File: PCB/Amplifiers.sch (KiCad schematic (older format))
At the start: 33 parts, among them U10 TL084_v, U11 LM358, U12 TL084_v

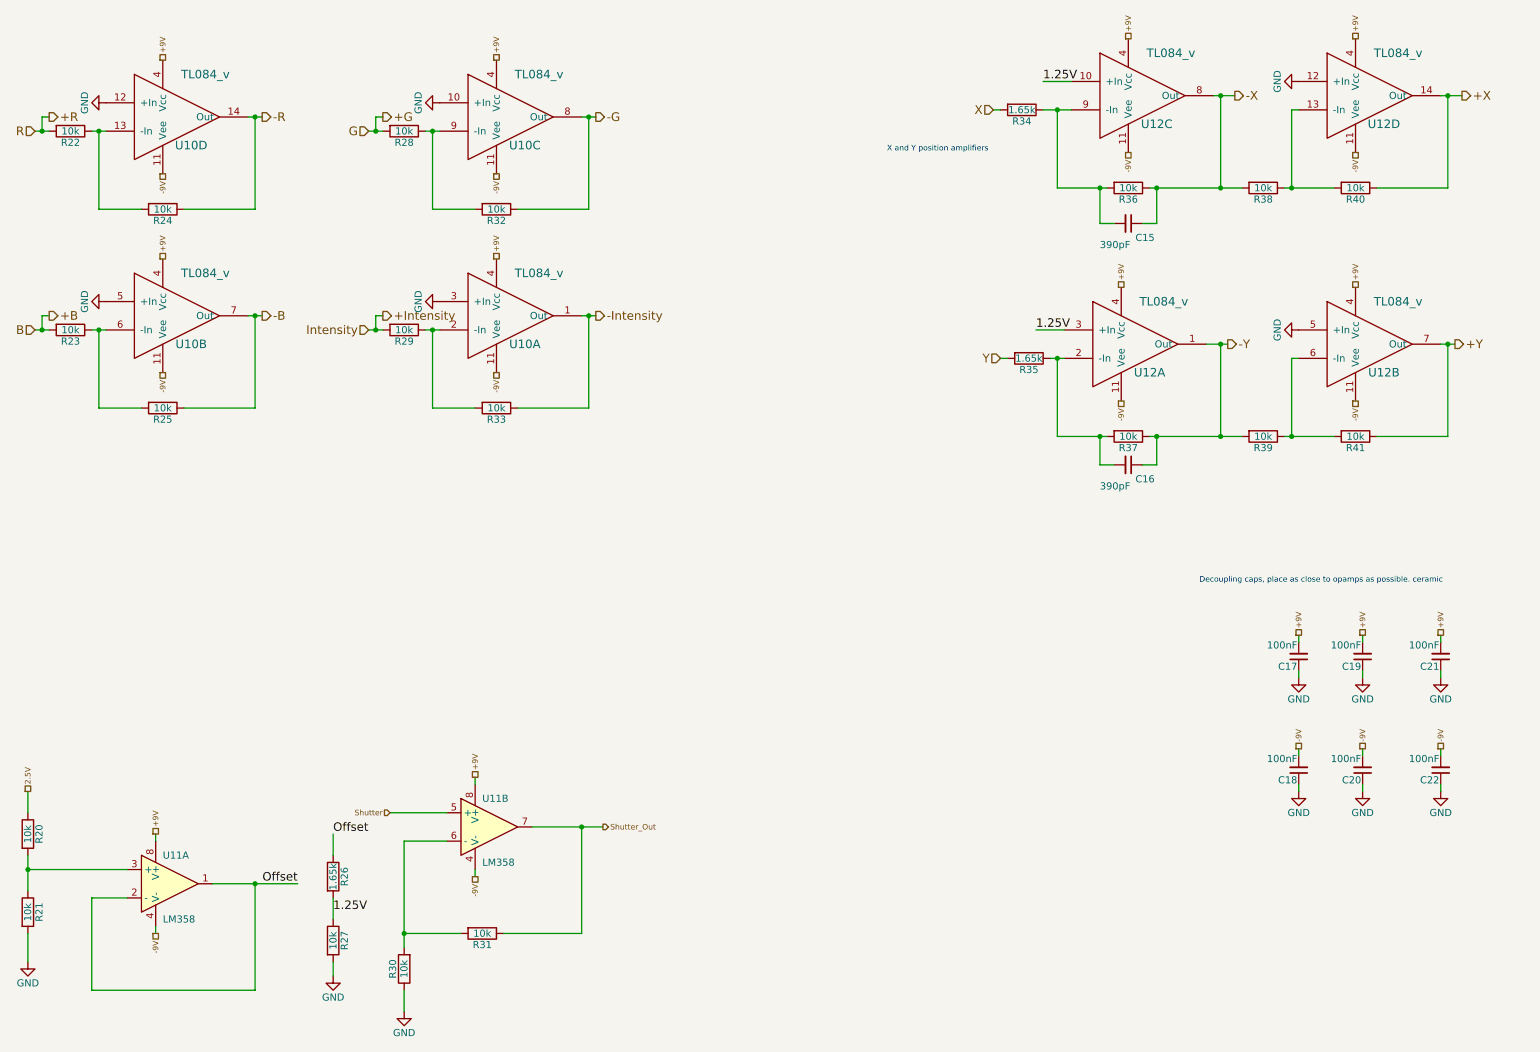
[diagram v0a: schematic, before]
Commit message: Generated BOM, fixed component names in schematic
Changed component names on output resistors and status LED to match that
in PCB
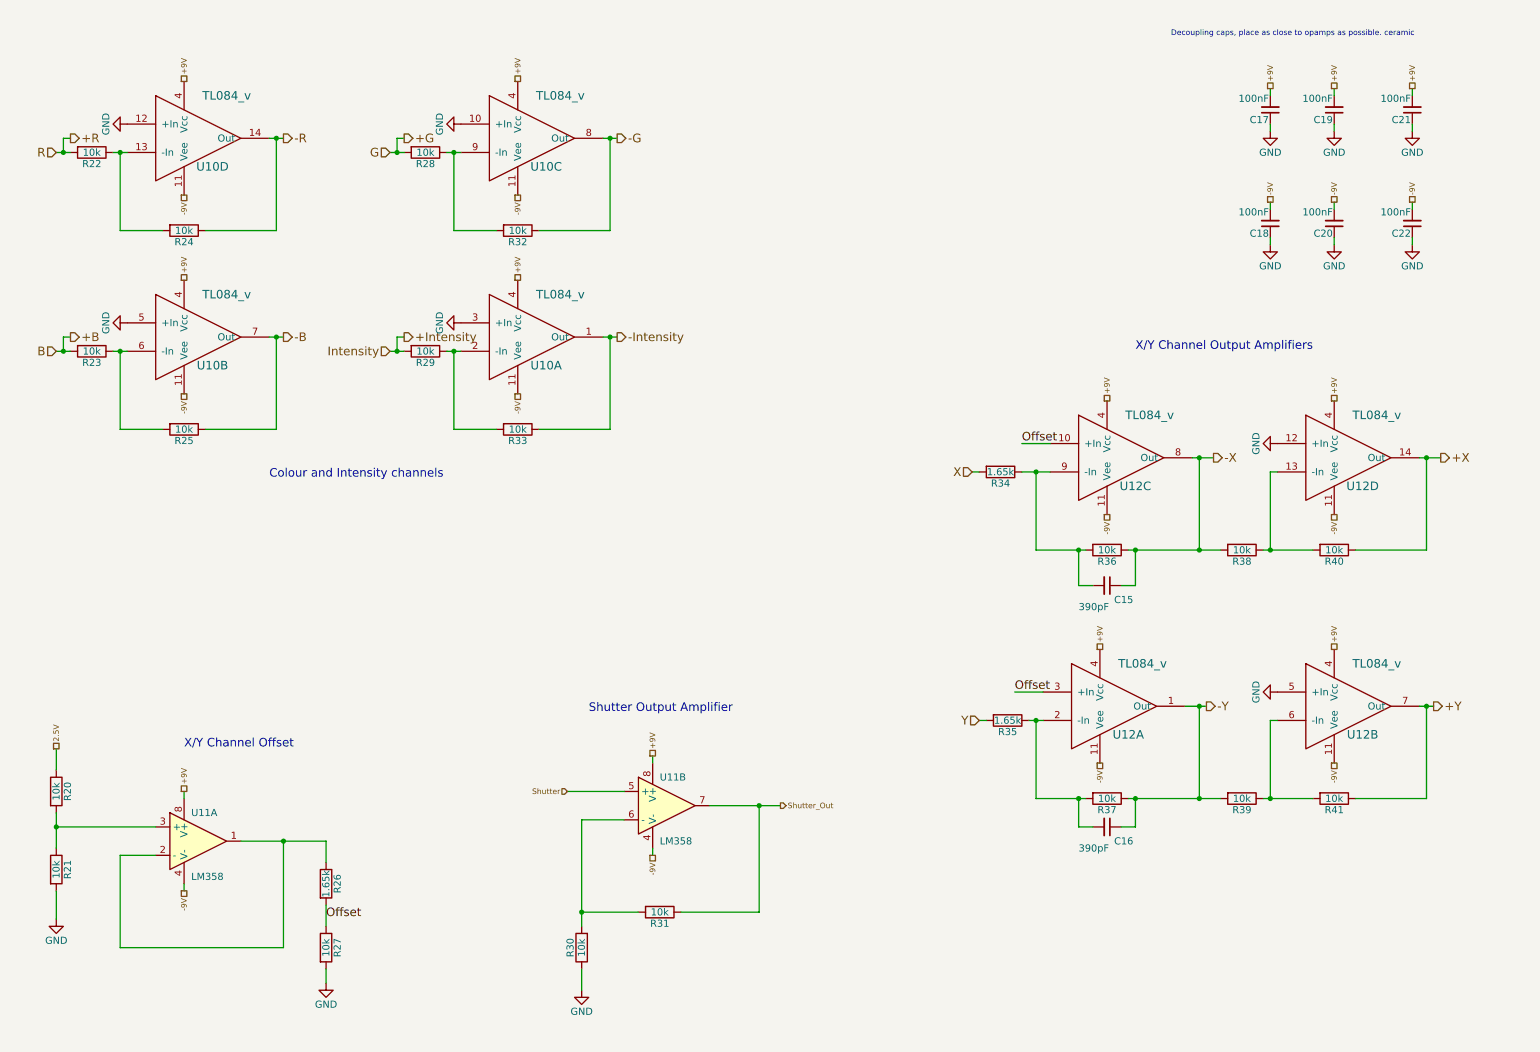
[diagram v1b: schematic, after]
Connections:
- net 1.25V is gone; now on net Offset: R26.2, R27.1, U12.10 (+In), U12.3 (+In)
- net Offset: no longer R26.1, U11.1, U11.2 (-)
- new net: R26.1, U11.1, U11.2 (-)
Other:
- note added: "Colour and Intensity channels\n"
- note added: "Shutter Output Amplifier\n"
- note added: "X/Y Channel Offset \n"
- note added: "X/Y Channel Output Amplifiers\n"
- note removed: "X and Y position amplifiers\n"
- moved on the sheet: C15, C16, C17, C18, C19, C20, C21, C22, R20, R21, R22, R23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

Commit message: Reannotated Components
Annotated components to standards,
TODO: Add Silkscreen for signals on bottom
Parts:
- renumbered C15 to C17, C16 to C18, C17 to C19, C18 to C20, C19 to C21, C20 to C22, C21 to C23, C22 to C24, R32 to R30, R33 to R31, R30 to R32, R31 to R33, U10 to U6, U11 to U7, U12 to U8
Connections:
- net +X: now also U8.8 (Out); no longer U8.14 (Out)
- net +Y: now also U8.14 (Out); no longer U8.7 (Out)
- net -Intensity: now also U6.14 (Out); no longer U6.1 (Out)
- net -R: now also U6.1 (Out); no longer U6.14 (Out)
- net -X: now also U8.7 (Out); no longer U8.8 (Out)
- net GND: now also U6.12 (+In), U6.3 (+In), U8.10 (+In), U8.12 (+In); no longer U6.12 (+In), U6.3 (+In), U8.12 (+In), U8.5 (+In)
- net Offset: now also U8.5 (+In); no longer U8.10 (+In)
- net at C17.2, R34.1, R36.2: now also U8.6 (-In); no longer U8.9 (-In)
- net at R39.1, R41.2: now also U8.13 (-In); no longer U8.6 (-In)
- net at R38.1, R40.2: now also U8.9 (-In); no longer U8.13 (-In)
- net at R22.1, R24.2: now also U6.2 (-In); no longer U6.13 (-In)
- net at R29.1, R31.2: now also U6.13 (-In); no longer U6.2 (-In)
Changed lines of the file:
@@
 $EndComp
 $Comp
-L R R31
+L R R33
 U 1 1 56D64139
 P 5150 6900
-F 0 "R31" V 5230 6900 50  0000 C CNN
+F 0 "R33" V 5230 6900 50  0000 C CNN
 F 1 "10k" V 5150 6900 50  0000 C CNN
 F 2 "Resistors_SMD:R_0805" V 5080 6900 50  0001 C CNN
@@
 $EndComp
 $Comp
-L R R30
+L R R32
 U 1 1 56D64552
 P 4600 7150
-F 0 "R30" V 4680 7150 50  0000 C CNN
+F 0 "R32" V 4680 7150 50  0000 C CNN
 F 1 "10k" V 4600 7150 50  0000 C CNN
 F 2 "Resistors_SMD:R_0805" V 4530 7150 50  0001 C CNN
@@
 -Y
 $Comp
-L TL084_v U12
+L TL084_v U8
 U 1 1 56E9E17A
 P 8200 5450
-F 0 "U12" H 8450 5250 60  0000 C CNN
+F 0 "U8" H 8450 5250 60  0000 C CNN
 F 1 "TL084_v" H 8550 5750 60  0000 C CNN
 F 2 "Housings_SSOP:TSSOP-14_4.4x5mm_Pitch0.65mm" H 8200 5450 60  0001 C CNN
@@
 $EndComp
 $Comp
-L TL084_v U12
-U 3 1 56E9E5C2
+L TL084_v U8
+U 2 1 56E9E5C2
 P 8250 3700
-F 0 "U12" H 8500 3500 60  0000 C CNN
+F 0 "U8" H 8500 3500 60  0000 C CNN
 F 1 "TL084_v" H 8600 4000 60  0000 C CNN
 F 2 "Housings_SSOP:TSSOP-14_4.4x5mm_Pitch0.65mm" H 8250 3700 60  0001 C CNN
 F 3 "" H 8250 3700 60  0000 C CNN
-	3    8250 3700
-	1    0    0    -1
-$EndComp
-$Comp
-L TL084_v U12
-U 2 1 56E9E60F
+	2    8250 3700
+	1    0    0    -1
+$EndComp
+$Comp
+L TL084_v U8
+U 4 1 56E9E60F
 P 9850 5450
-F 0 "U12" H 10100 5250 60  0000 C CNN
+F 0 "U8" H 10100 5250 60  0000 C CNN
 F 1 "TL084_v" H 10200 5750 60  0000 C CNN
 F 2 "Housings_SSOP:TSSOP-14_4.4x5mm_Pitch0.65mm" H 9850 5450 60  0001 C CNN
 F 3 "" H 9850 5450 60  0000 C CNN
-	2    9850 5450
-	1    0    0    -1
-$EndComp
-$Comp
-L TL084_v U12
-U 4 1 56E9E664
+	4    9850 5450
+	1    0    0    -1
+$EndComp
+$Comp
+L TL084_v U8
+U 3 1 56E9E664
 P 9850 3700
-F 0 "U12" H 10100 3500 60  0000 C CNN
+F 0 "U8" H 10100 3500 60  0000 C CNN
 F 1 "TL084_v" H 10200 4000 60  0000 C CNN
 F 2 "Housings_SSOP:TSSOP-14_4.4x5mm_Pitch0.65mm" H 9850 3700 60  0001 C CNN
 F 3 "" H 9850 3700 60  0000 C CNN
-	4    9850 3700
+	3    9850 3700
 	1    0    0    -1
 $EndComp
@@
 $EndComp
 $Comp
-L R R32
+L R R30
 U 1 1 56EAB260
 P 4150 2100
-F 0 "R32" V 4230 2100 50  0000 C CNN
+F 0 "R30" V 4230 2100 50  0000 C CNN
 F 1 "10k" V 4150 2100 50  0000 C CNN
 F 2 "Resistors_SMD:R_0805" V 4080 2100 50  0001 C CNN
@@
 	3650 2950 3750 2950
 $Comp
-L R R33
+L R R31
 U 1 1 56EAD91A
 P 4150 3500
-F 0 "R33" V 4230 3500 50  0000 C CNN
+F 0 "R31" V 4230 3500 50  0000 C CNN
 F 1 "10k" V 4150 3500 50  0000 C CNN
 F 2 "Resistors_SMD:R_0805" V 4080 3500 50  0001 C CNN
@@
 -9V
 $Comp
-L C_Small C17
+L C_Small C19
 U 1 1 56ECBD65
 P 9450 1250
-F 0 "C17" H 9460 1320 50  0000 L CNN
+F 0 "C19" H 9460 1320 50  0000 L CNN
 F 1 "100nF" H 9460 1170 50  0000 L CNN
 F 2 "Capacitors_SMD:C_0402" H 9450 1250 50  0001 C CNN
@@
 +9V
 $Comp
-L C_Small C19
+L C_Small C21
 U 1 1 56ECC944
 P 9900 1250
-F 0 "C19" H 9910 1320 50  0000 L CNN
+F 0 "C21" H 9910 1320 50  0000 L CNN
 F 1 "100nF" H 9910 1170 50  0000 L CNN
 F 2 "Capacitors_SMD:C_0402" H 9900 1250 50  0001 C CNN
@@
 $EndComp
 $Comp
-L C_Small C21
+L C_Small C23
 U 1 1 56ECC9C0
 P 10450 1250
-F 0 "C21" H 10460 1320 50  0000 L CNN
+F 0 "C23" H 10460 1320 50  0000 L CNN
 F 1 "100nF" H 10460 1170 50  0000 L CNN
 F 2 "Capacitors_SMD:C_0402" H 10450 1250 50  0001 C CNN
@@
 	10450 1100 10450 1150
 $Comp
-L C_Small C18
+L C_Small C20
 U 1 1 56ECD04E
 P 9450 2050
-F 0 "C18" H 9460 2120 50  0000 L CNN
+F 0 "C20" H 9460 2120 50  0000 L CNN
 F 1 "100nF" H 9460 1970 50  0000 L CNN
 F 2 "Capacitors_SMD:C_0402" H 9450 2050 50  0001 C CNN
@@
 $EndComp
 $Comp
-L C_Small C20
+L C_Small C22
 U 1 1 56ECD054
 P 9900 2050
-F 0 "C20" H 9910 2120 50  0000 L CNN
+F 0 "C22" H 9910 2120 50  0000 L CNN
 F 1 "100nF" H 9910 1970 50  0000 L CNN
 F 2 "Capacitors_SMD:C_0402" H 9900 2050 50  0001 C CNN
@@
 $EndComp
 $Comp
-L C_Small C22
+L C_Small C24
 U 1 1 56ECD05A
 P 10450 2050
-F 0 "C22" H 10460 2120 50  0000 L CNN
+F 0 "C24" H 10460 2120 50  0000 L CNN
 F 1 "100nF" H 10460 1970 50  0000 L CNN
 F 2 "Capacitors_SMD:C_0402" H 10450 2050 50  0001 C CNN
@@
 Decoupling caps, place as close to opamps as possible. ceramic\n\n
 $Comp
-L C_Small C15
+L C_Small C17
 U 1 1 56FC5661
 P 8300 4600
-F 0 "C15" V 8400 4650 50  0000 L CNN
+F 0 "C17" V 8400 4650 50  0000 L CNN
 F 1 "390pF" V 8450 4400 50  0000 L CNN
 F 2 "Capacitors_SMD:C_0402" H 8300 4600 50  0001 C CNN
@@
 Connection ~ 8500 4350
 $Comp
-L C_Small C16
+L C_Small C18
 U 1 1 56FC5BD0
 P 8300 6300
-F 0 "C16" V 8400 6350 50  0000 L CNN
+F 0 "C18" V 8400 6350 50  0000 L CNN
 F 1 "390pF" V 8450 6100 50  0000 L CNN
 F 2 "Capacitors_SMD:C_0402" H 8300 6300 50  0001 C CNN
@@
 Connection ~ 8500 6100
 $Comp
-L LM358 U11
+L LM358 U7
 U 1 1 56FC6EA1
 P 1900 6400
-F 0 "U11" H 1850 6600 50  0000 L CNN
+F 0 "U7" H 1850 6600 50  0000 L CNN
 F 1 "LM358" H 1850 6150 50  0000 L CNN
 F 2 "Housings_SOIC:SOIC-8_3.9x4.9mm_Pitch1.27mm" H 1900 6400 50  0001 C CNN
@@
 $EndComp
 $Comp
-L LM358 U11
+L LM358 U7
 U 2 1 56FC6F7E
 P 5200 6150
-F 0 "U11" H 5150 6350 50  0000 L CNN
+F 0 "U7" H 5150 6350 50  0000 L CNN
 F 1 "LM358" H 5150 5900 50  0000 L CNN
 F 2 "Housings_SOIC:SOIC-8_3.9x4.9mm_Pitch1.27mm" H 5200 6150 50  0001 C CNN
@@
 $EndComp
 $Comp
-L TL084_v U10
-U 1 1 56FAD544
+L TL084_v U6
+U 4 1 56FAD544
 P 4100 2850
-F 0 "U10" H 4350 2650 60  0000 C CNN
+F 0 "U6" H 4350 2650 60  0000 C CNN
 F 1 "TL084_v" H 4450 3150 60  0000 C CNN
 F 2 "Housings_SSOP:TSSOP-14_4.4x5mm_Pitch0.65mm" H 4100 2850 60  0001 C CNN
 F 3 "" H 4100 2850 60  0000 C CNN
-	1    4100 2850
-	1    0    0    -1
-$EndComp
-$Comp
-L TL084_v U10
+	4    4100 2850
+	1    0    0    -1
+$EndComp
+$Comp
+L TL084_v U6
 U 3 1 56FAD5F9
 P 4100 1450
-F 0 "U10" H 4350 1250 60  0000 C CNN
+F 0 "U6" H 4350 1250 60  0000 C CNN
 F 1 "TL084_v" H 4450 1750 60  0000 C CNN
 F 2 "Housings_SSOP:TSSOP-14_4.4x5mm_Pitch0.65mm" H 4100 1450 60  0001 C CNN
@@
 $EndComp
 $Comp
-L TL084_v U10
+L TL084_v U6
 U 2 1 56FAD674
 P 1750 2850
-F 0 "U10" H 2000 2650 60  0000 C CNN
+F 0 "U6" H 2000 2650 60  0000 C CNN
 F 1 "TL084_v" H 2100 3150 60  0000 C CNN
 F 2 "Housings_SSOP:TSSOP-14_4.4x5mm_Pitch0.65mm" H 1750 2850 60  0001 C CNN
@@
 $EndComp
 $Comp
-L TL084_v U10
-U 4 1 56FAD745
+L TL084_v U6
+U 1 1 56FAD745
 P 1750 1450
-F 0 "U10" H 2000 1250 60  0000 C CNN
+F 0 "U6" H 2000 1250 60  0000 C CNN
 F 1 "TL084_v" H 2100 1750 60  0000 C CNN
 F 2 "Housings_SSOP:TSSOP-14_4.4x5mm_Pitch0.65mm" H 1750 1450 60  0001 C CNN
 F 3 "" H 1750 1450 60  0000 C CNN
-	4    1750 1450
-	1    0    0    -1
-$EndComp
+	1    1750 1450
+	1    0    0    -1
+$EndComp
